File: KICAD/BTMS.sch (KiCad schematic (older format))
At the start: 316 parts, among them J1 fan, J10 U1COMMS, J11 U2COMMS, J13 IntBTemp, J14 ctrlTemp, J15 12Vout, J16 12Vin, J17 5Vout, J2 mContactor, J3 Tac, J5 ICSP, J7 5Vout, J9 key, Q1 PSMN5R6-100BS, Q10 PSMN5R6-100BS, Q11 DMN65D8L, Q12 DMN65D8L, Q13 FDN340P, Q14 ZXTP2025FTA, Q15 ZXTP2025FTA, Q16 ZXTP2025FTA, Q17 DMN65D8L, Q18 DMN65D8L, Q2 PSMN5R6-100BS, Q3 PSMN5R6-100BS, Q4 DMN65D8L, Q5 DMN65D8L, Q6 DMN65D8L, Q7 DMN65D8L, Q8 PSMN5R6-100BS, Q9 FDN340P, U1 R-78HB12-0.5, U10 A41AS12VDC, U11 A41AS12VDC, U12 A41AS12VDC, U13 A41AS12VDC, U14 A41AS12VDC, U15 NL17SZ74USG, U2 ACS780xLRTR-050B, U3 UCC27201DDAR, U4 FAN3111ESX, U5 HCPL-3120, U6 L7805CV, U7 LTV-817S, U8 dsPIC30F3011-PT, U9 LM62CIM3/NOPB

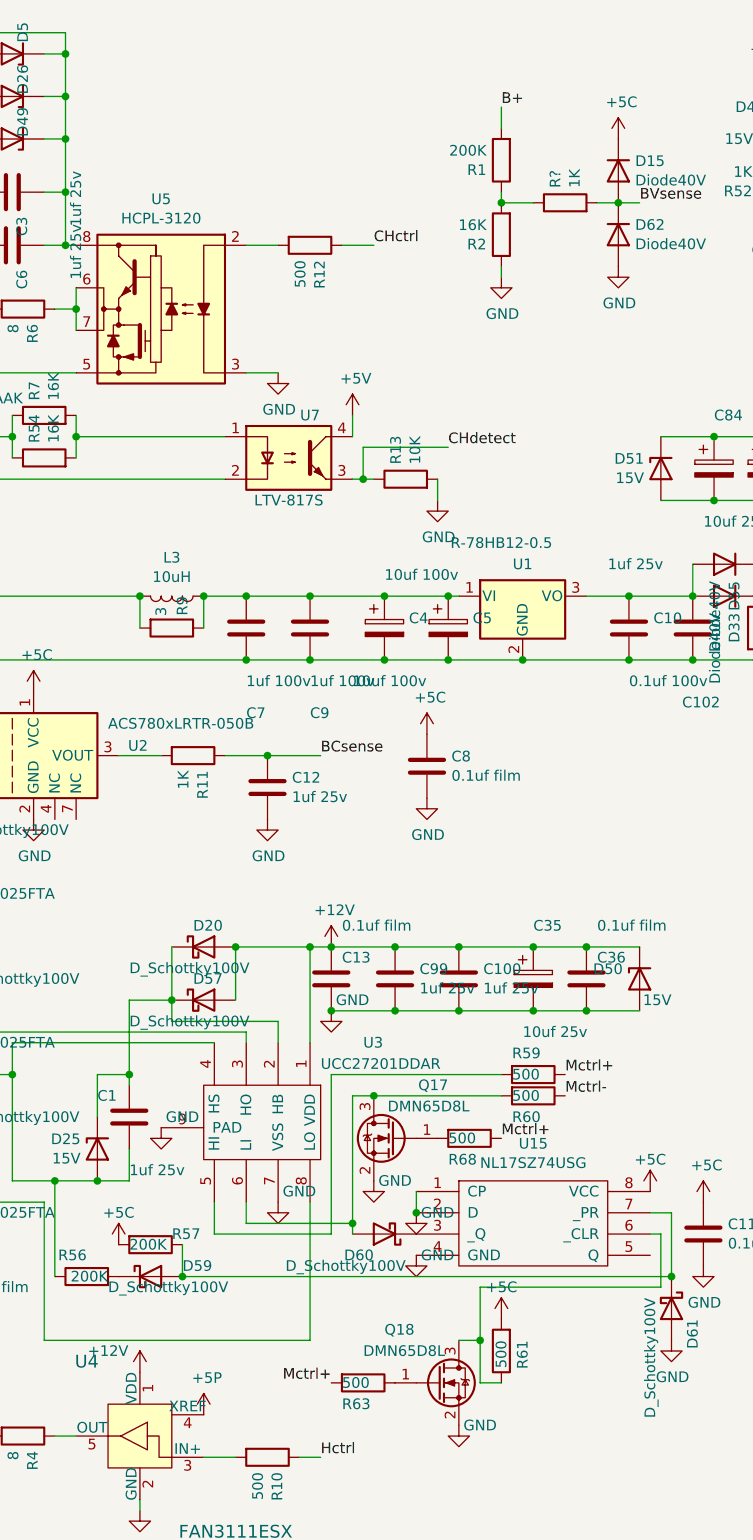
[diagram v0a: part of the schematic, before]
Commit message: Fixed a mislabeled net; changed from 5vP to 5vC on U4. Need to update board layout; changed some capacitors and other previously noted schematic changes.
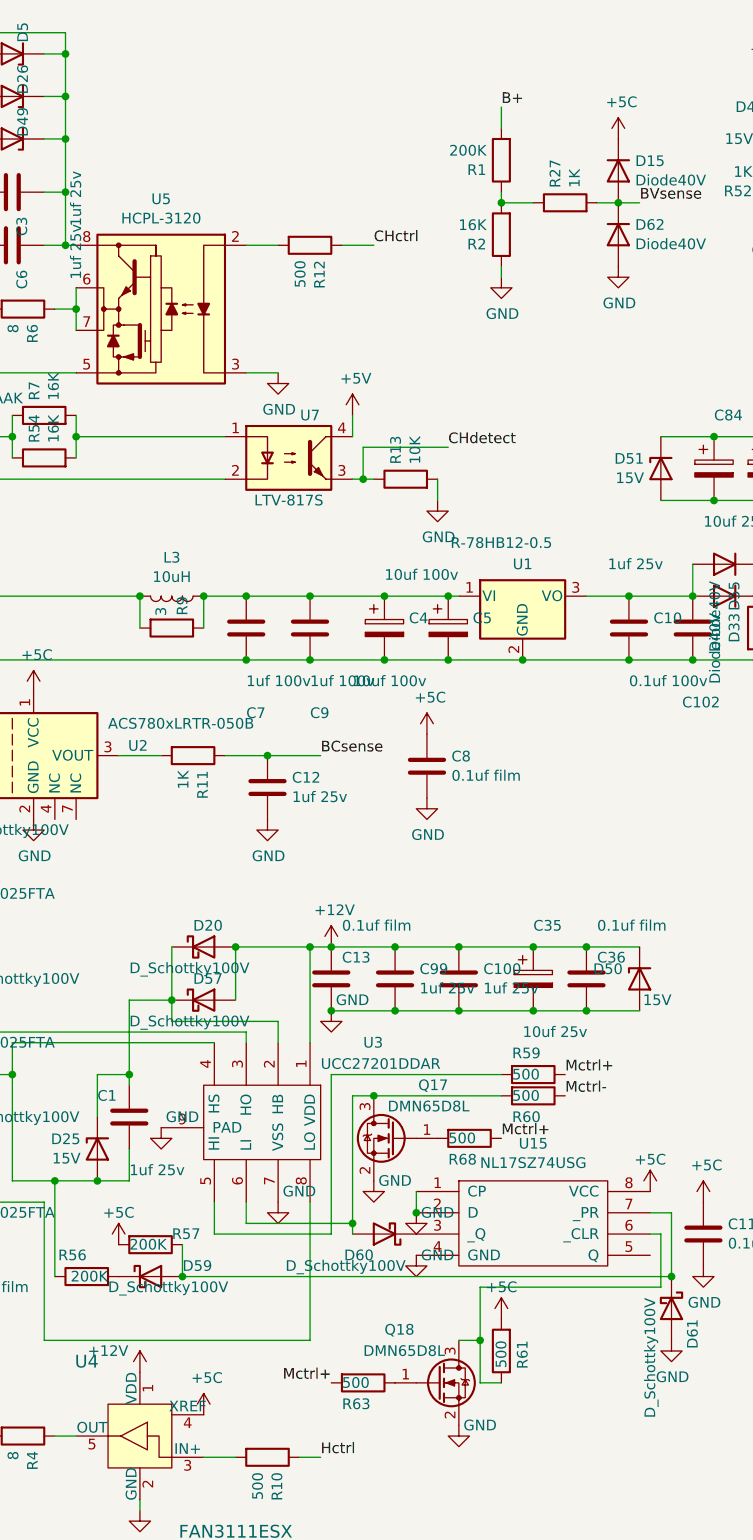
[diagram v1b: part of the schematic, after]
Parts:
- gave numbers to parts that had none: 1
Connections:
- net +5P is gone; now on net +5C: U4.4 (XREF)
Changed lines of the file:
@@
 	5350 8400 5700 8400
 $Comp
-L power:+5P #PWR0131
-U 1 1 6047FC08
-P 3950 7000
-F 0 "#PWR0131" H 3950 6850 50  0001 C CNN
-F 1 "+5P" H 3965 7173 50  0000 C CNN
-F 2 "" H 3950 7000 50  0001 C CNN
-F 3 "" H 3950 7000 50  0001 C CNN
-	1    3950 7000
-	1    0    0    -1
-$EndComp
-$Comp
 L Device:R R49
 U 1 1 60481A16
@@
 $EndComp
 $Comp
-L Device:R R?
+L Device:R R27
 U 1 1 62134C51
 P 5650 1300
-F 0 "R?" H 5720 1346 50  0000 L CNN
+F 0 "R27" H 5720 1346 50  0000 L CNN
 F 1 "1K" H 5720 1255 50  0000 L CNN
 F 2 "Resistors_SMD:R_0603" V 5580 1300 50  0001 C CNN
@@
 	0    -1   -1   0
 $EndComp
+$Comp
+L power:+5C #PWR?
+U 1 1 6212B3B2
+P 3950 7000
+F 0 "#PWR?" H 3950 6850 50  0001 C CNN
+F 1 "+5C" H 3965 7173 50  0000 C CNN
+F 2 "" H 3950 7000 50  0001 C CNN
+F 3 "" H 3950 7000 50  0001 C CNN
+	1    3950 7000
+	1    0    0    -1
+$EndComp
 $EndSCHEMATC

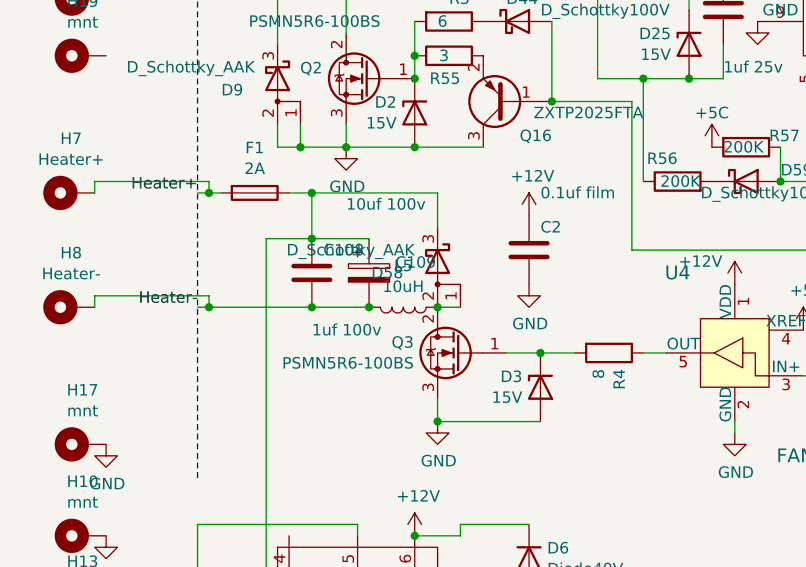
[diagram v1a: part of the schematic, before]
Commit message: Updated readme to list current state of project.
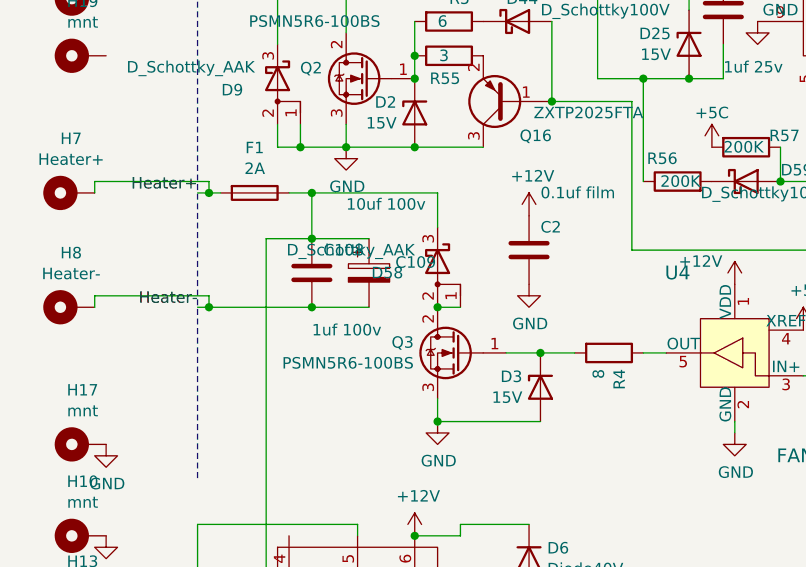
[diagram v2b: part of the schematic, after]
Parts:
- removed L5: 10uH, Inductors:Inductor_Wurth_HCI-5040, symbol Device:L
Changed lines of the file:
@@
 Connection ~ 2350 7400
-$Comp
-L Device:L L5
-U 1 1 602155FB
-P 2200 6900
-F 0 "L5" V 2019 6900 50  0000 C CNN
-F 1 "10uH" V 2110 6900 50  0000 C CNN
-F 2 "Inductors:Inductor_Wurth_HCI-5040" H 2200 6900 50  0001 C CNN
-F 3 "~" H 2200 6900 50  0001 C CNN
-F 4 "https://www.digikey.com/en/products/detail/w%C3%BCrth-elektronik/74404054100/4865412" H 2200 6900 50  0001 C CNN "DK_Detail_Page"
-F 5 "732-5519-1-ND" H 2200 6900 50  0001 C CNN "Digi-Key_PN"
-	1    2200 6900
-	0    1    1    0
-$EndComp
 $Comp
 L Device:CP C109
@@
 Wire Wire Line
 	1800 6900 2050 6900
-Connection ~ 2050 6900
 Wire Wire Line
 	2050 6600 1800 6600

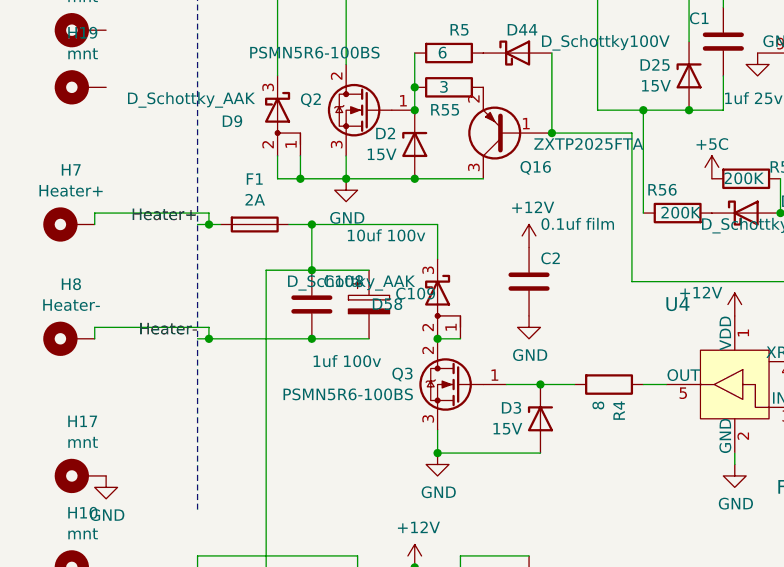
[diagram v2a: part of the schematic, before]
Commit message: Major refactoring, and optimizations. Added some groundwork for custom serial port displays. NEW BUGS: Serial ports hang for some unknown reason. Heatcal gets ran multiple times when charger is plugged in. Heat doesn't always run when supposed to. Heater relay doesn't always turn off when it's not needed. And possibly more!
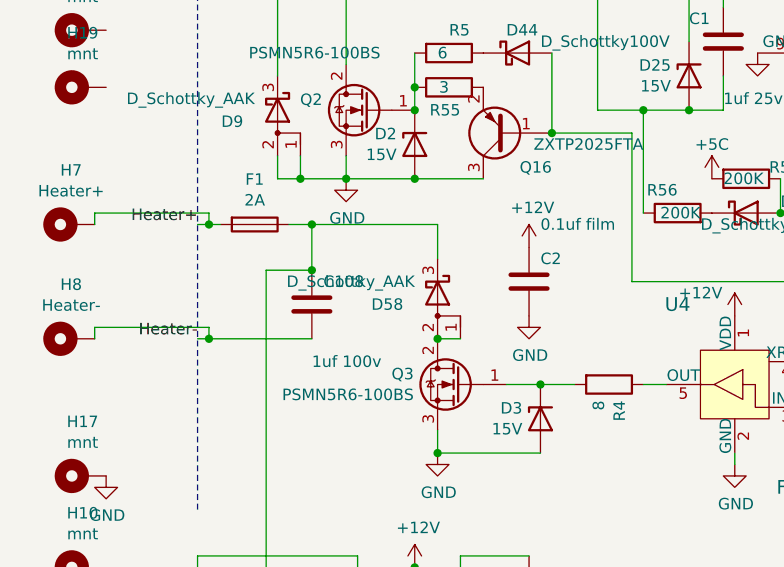
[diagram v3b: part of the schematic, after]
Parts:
- removed C109: 10uf 100v, Capacitors_SMD:C_1210, symbol Device:CP
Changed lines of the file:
@@
 Connection ~ 2350 7400
-$Comp
-L Device:CP C109
-U 1 1 60218595
-P 2050 6750
-F 0 "C109" H 2165 6796 50  0000 L CNN
-F 1 "10uf 100v" H 1950 7050 50  0000 L CNN
-F 2 "Capacitors_SMD:C_1210" H 2088 6600 50  0001 C CNN
-F 3 "~" H 2050 6750 50  0001 C CNN
-F 4 "https://www.digikey.com/en/products/detail/murata-electronics/GRM32EC72A106KE05L/7319356" H 2050 6750 50  0001 C CNN "DK_Detail_Page"
-F 5 "490-16266-1-ND" H 2050 6750 50  0001 C CNN "Digi-Key_PN"
-	1    2050 6750
-	1    0    0    -1
-$EndComp
 $Comp
 L Device:C C108
@@
 	1    0    0    -1
 $EndComp
-Connection ~ 1800 6900
 Wire Wire Line
 	1800 6900 1350 6900
 Wire Wire Line
-	1800 6900 2050 6900
-Wire Wire Line
-	2050 6600 1800 6600
-Wire Wire Line
 	1800 6600 1600 6600
